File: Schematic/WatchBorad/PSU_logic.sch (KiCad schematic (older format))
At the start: 32 parts, among them J3 TYPE-C-31-M-17, SW1 SW_Push, SW2 SW_Push, U5 BQ21040DBVT, U6 MAX17048G+T10, U7 max16054azt+t, U8 TPS2113APWR

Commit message: Added missed footprints
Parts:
- U6: footprint 21-0168E_T822-3_MXM -> LocalFootprints:MAX17048G
- U8: footprint PowerMuxesFP:TPS2115APWR -> LocalFootprints:TPS2115APWR
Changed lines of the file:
@@
 F 0 "U6" H 4725 6712 60  0000 C CNN
 F 1 "MAX17048G+T10" H 4725 6606 60  0000 C CNN
-F 2 "21-0168E_T822-3_MXM" H 4700 6575 60  0001 C CNN
+F 2 "LocalFootprints:MAX17048G" H 4700 6575 60  0001 C CNN
 F 3 "https://datasheet.lcsc.com/lcsc/2106070437_Maxim-Integrated-MAX17048G-T10_C2682616.pdf" H 4725 6606 60  0001 C CNN
 F 4 "https://lcsc.com/product-detail/PMIC-Battery-Management_Maxim-Integrated-MAX17048G-T10_C2682616.html" H 3925 6325 50  0001 C CNN "lcsc"
@@
 F 0 "U8" H 8375 5062 60  0000 C CNN
 F 1 "TPS2113APWR" H 8375 4956 60  0000 C CNN
-F 2 "PowerMuxesFP:TPS2115APWR" H 8375 4915 60  0001 C CNN
+F 2 "LocalFootprints:TPS2115APWR" H 8375 4915 60  0001 C CNN
 F 3 "https://datasheet.lcsc.com/lcsc/Texas-Instruments-TI-TPS2113APWR_C130052.pdf" H 8375 4175 60  0001 C CNN
 F 4 "https://lcsc.com/product-detail/PMIC-Power-Distribution-Switches_Texas-Instruments_TPS2113APWR_Texas-Instruments-Texas-Instruments-TPS2113APWR_C130052.html" H 8375 4425 50  0001 C CNN "lcsc"

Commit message: Added battery print
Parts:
- BT1: footprint Battery_Holders:Keystone_107_1x23mm-CoinCell -> LocalFootprints:BatteryPads
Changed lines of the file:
@@
 F 0 "BT1" H 1218 6746 50  0000 L CNN
 F 1 "Battery_Cell" H 1218 6655 50  0000 L CNN
-F 2 "Battery_Holders:Keystone_107_1x23mm-CoinCell" V 1100 6710 50  0001 C CNN
+F 2 "LocalFootprints:BatteryPads" V 1100 6710 50  0001 C CNN
 F 3 "https://aliexpress.ru/item/33000396152.html?spm=a2g0o.productlist.0.0.43416af464CXwu&algo_pvid=e6706777-cde6-4668-9867-8799ba4921bb&algo_expid=e6706777-cde6-4668-9867-8799ba4921bb-0&btsid=0b8b037215874644191236041ea897&ws_ab_test=searchweb0_0,searchweb201602_,searchweb201603_" V 1100 6710 50  0001 C CNN
 	1    1100 6650

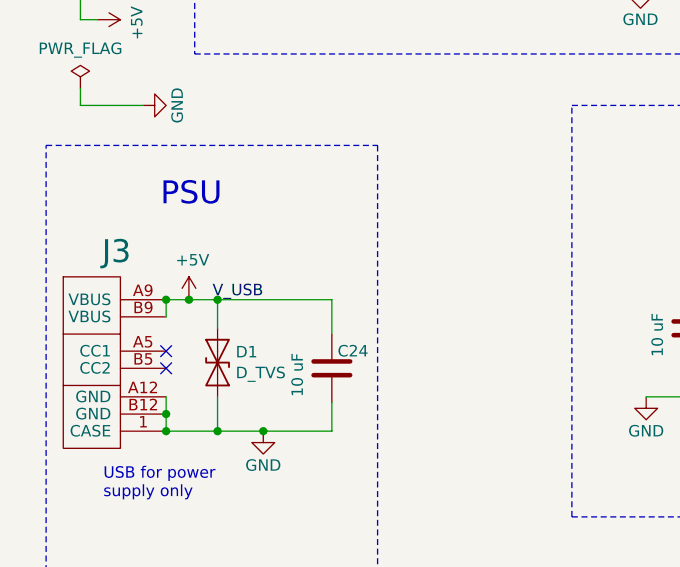
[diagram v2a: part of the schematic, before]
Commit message: Fixed board's proposals. Fixed testpoints' footprint. Fixed DRC violations. Added +5V testpoint
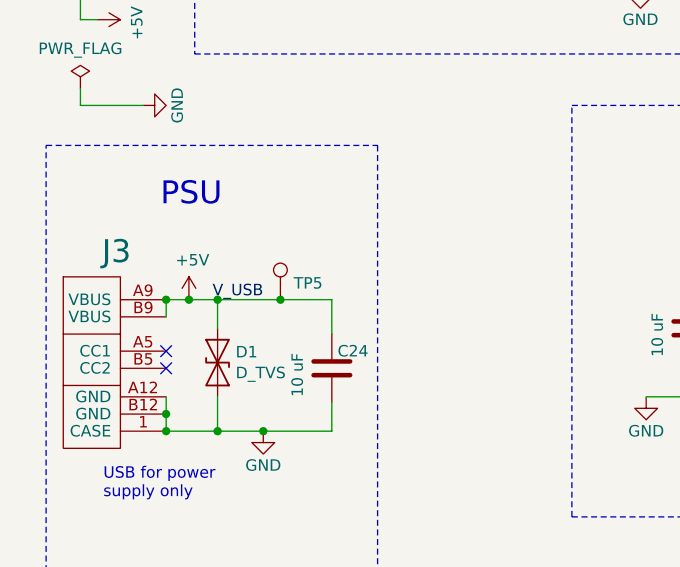
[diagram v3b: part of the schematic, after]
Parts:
- added TP5: TestPoint, TestPoint:TestPoint_Pad_D2.0mm, symbol Connector:TestPoint
- TP11, TP12: footprint Measurement_Points:Measurement_Point_Round-SMD-Pad_Small -> TestPoint:TestPoint_Pad_D2.0mm
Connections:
- wire segments 130 -> 131
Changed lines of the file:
@@
 F 0 "TP11" H 7633 1847 50  0000 L CNN
 F 1 "TestPoint" H 7633 1802 50  0001 L CNN
-F 2 "Measurement_Points:Measurement_Point_Round-SMD-Pad_Small" H 7775 1775 50  0001 C CNN
+F 2 "TestPoint:TestPoint_Pad_D2.0mm" H 7775 1775 50  0001 C CNN
 F 3 "~" H 7775 1775 50  0001 C CNN
 	1    7575 1775
@@
 F 0 "TP12" H 9858 4147 50  0000 L CNN
 F 1 "TestPoint" H 9858 4102 50  0001 L CNN
-F 2 "Measurement_Points:Measurement_Point_Round-SMD-Pad_Small" H 10000 4075 50  0001 C CNN
+F 2 "TestPoint:TestPoint_Pad_D2.0mm" H 10000 4075 50  0001 C CNN
 F 3 "~" H 10000 4075 50  0001 C CNN
 	1    9800 4075
@@
 	1775 4250 1775 4400
 Wire Wire Line
-	1275 4250 1775 4250
+	1275 4250 1550 4250
 $Comp
 L Device:C C?
@@
 	9200 4575 9200 4675
 Connection ~ 9200 4675
+$Comp
+L Connector:TestPoint TP?
+U 1 1 60EA81F2
+P 1550 4250
+AR Path="/5E9C1C3A/60EA81F2" Ref="TP?"  Part="1"
+AR Path="/5ED3F98E/60EA81F2" Ref="TP?"  Part="1"
+AR Path="/5F913559/60EA81F2" Ref="TP5"  Part="1"
+F 0 "TP5" H 1608 4322 50  0000 L CNN
+F 1 "TestPoint" H 1608 4277 50  0001 L CNN
+F 2 "TestPoint:TestPoint_Pad_D2.0mm" H 1750 4250 50  0001 C CNN
+F 3 "~" H 1750 4250 50  0001 C CNN
+	1    1550 4250
+	1    0    0    -1
+$EndComp
+Connection ~ 1550 4250
+Wire Wire Line
+	1550 4250 1775 4250
 $EndSCHEMATC

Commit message: Added new DCDC and radio antenna from Rulepas [SCHECMATIC]
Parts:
- removed R25: 10k, Resistor_SMD:R_0603_1608Metric, symbol Device:R
- removed VT3: HX2301A, TO_SOT_Packages_SMD:SOT-23, symbol MosfetLocal:HX2301A
- added C?: 100 nF, Capacitor_SMD:C_0603_1608Metric, symbol Device:C
- added R? (x2): 10k, Resistor_SMD:R_0603_1608Metric, symbol Device:R
- added U?: M41T62Q6F, QFN50P300X300X100-17N, symbol M41T62Q6F:M41T62Q6F
- added Y?: Crystal_Small, Crystal:Crystal_SMD_3215-2Pin_3.2x1.5mm, symbol Device:Crystal_Small
- U6: symbol WatchBorad-rescue:MAX17048G+T10-BatteryManagmentLocal-WatchBorad-rescue -> WatchBorad-rescue:MAX17048G+T10-BatteryManagmentLocal-WatchBorad-rescue-WatchBorad-rescue
- U8: symbol WatchBorad-rescue:TPS2113APWR-PowerMuxes-WatchBorad-rescue -> WatchBorad-rescue:TPS2113APWR-PowerMuxes-WatchBorad-rescue-WatchBorad-rescue
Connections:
- net labels added: I2C_SCL_STBY, I2C_SDA_STBY, PWR_SW_EN_N, XI_RTC, XO_RTC
- net labels removed: V_Battery_P_SW
- wire segments 131 -> 145
- no-connect marks 5 -> 7
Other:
- note added: "32.768 KHz\n"
- note added: "RTC_I2C"
- note added: "default level is "0""
- note added: "internal PU\n"
- note removed: "PUs next to MCU\n"
- moved on the sheet: C25, C26, C28, C29, C30, C31, R15, R16, R17, R18, R20, R21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

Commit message: Added schematic files annotations [SCHEMATIC]
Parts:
- gave numbers to parts that had none: 5
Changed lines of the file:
@@
 P 8225 4200
 AR Path="/5E9B1DCE/61A98A66" Ref="#PWR?"  Part="1"
-AR Path="/5F913559/61A98A66" Ref="#PWR?"  Part="1"
-F 0 "#PWR?" H 8225 3950 50  0001 C CNN
+AR Path="/5F913559/61A98A66" Ref="#PWR07"  Part="1"
+F 0 "#PWR07" H 8225 3950 50  0001 C CNN
 F 1 "GND" H 8230 4027 50  0000 C CNN
 F 2 "" H 8225 4200 50  0001 C CNN
@@
 P 9475 3050
 AR Path="/5E9B1DCE/61A98A80" Ref="U?"  Part="1"
-AR Path="/5F913559/61A98A80" Ref="U?"  Part="1"
-F 0 "U?" H 9475 4220 50  0000 C CNN
+AR Path="/5F913559/61A98A80" Ref="U10"  Part="1"
+F 0 "U10" H 9475 4220 50  0000 C CNN
 F 1 "M41T62Q6F" H 9475 4129 50  0000 C CNN
 F 2 "QFN50P300X300X100-17N" H 9475 3050 50  0001 L BNN
@@
 P 10325 3600
 AR Path="/5E9B1DCE/61A98A89" Ref="#PWR?"  Part="1"
-AR Path="/5F913559/61A98A89" Ref="#PWR?"  Part="1"
-F 0 "#PWR?" H 10325 3350 50  0001 C CNN
+AR Path="/5F913559/61A98A89" Ref="#PWR051"  Part="1"
+F 0 "#PWR051" H 10325 3350 50  0001 C CNN
 F 1 "GND" H 10330 3427 50  0000 C CNN
 F 2 "" H 10325 3600 50  0001 C CNN
@@
 AR Path="/5E9B1DCE/61A98A8F" Ref="C?"  Part="1"
 AR Path="/61A98A8F" Ref="C?"  Part="1"
-AR Path="/5F913559/61A98A8F" Ref="C?"  Part="1"
-F 0 "C?" H 10500 3400 50  0000 L CNN
+AR Path="/5F913559/61A98A8F" Ref="C6"  Part="1"
+F 0 "C6" H 10500 3400 50  0000 L CNN
 F 1 "100 nF" H 10450 3300 50  0000 L CNN
 F 2 "Capacitor_SMD:C_0603_1608Metric" H 10363 3225 50  0001 C CNN
@@
 P 10375 2400
 AR Path="/5E9B1DCE/61A98AAA" Ref="R?"  Part="1"
-AR Path="/5F913559/61A98AAA" Ref="R?"  Part="1"
-F 0 "R?" H 10445 2446 50  0000 L CNN
+AR Path="/5F913559/61A98AAA" Ref="R2"  Part="1"
+F 0 "R2" H 10445 2446 50  0000 L CNN
 F 1 "10k" H 10445 2355 50  0000 L CNN
 F 2 "Resistor_SMD:R_0603_1608Metric" V 10305 2400 50  0001 C CNN
@@
 P 8325 2300
 AR Path="/5E9B1DCE/61A98AB0" Ref="R?"  Part="1"
-AR Path="/5F913559/61A98AB0" Ref="R?"  Part="1"
-F 0 "R?" H 8395 2346 50  0000 L CNN
+AR Path="/5F913559/61A98AB0" Ref="R1"  Part="1"
+F 0 "R1" H 8395 2346 50  0000 L CNN
 F 1 "10k" H 8395 2255 50  0000 L CNN
 F 2 "Resistor_SMD:R_0603_1608Metric" V 8255 2300 50  0001 C CNN
@@
 AR Path="/5F7F86D0/61AF93FF" Ref="#PWR?"  Part="1"
 AR Path="/5ED3F98E/61AF93FF" Ref="#PWR?"  Part="1"
-AR Path="/5F913559/61AF93FF" Ref="#PWR?"  Part="1"
-F 0 "#PWR?" H 8625 1950 50  0001 C CNN
+AR Path="/5F913559/61AF93FF" Ref="#PWR012"  Part="1"
+F 0 "#PWR012" H 8625 1950 50  0001 C CNN
 F 1 "+BATT" H 8640 2273 50  0000 C CNN
 F 2 "" H 8625 2100 50  0001 C CNN
@@
 AR Path="/5F7F86D0/61AFA253" Ref="#PWR?"  Part="1"
 AR Path="/5ED3F98E/61AFA253" Ref="#PWR?"  Part="1"
-AR Path="/5F913559/61AFA253" Ref="#PWR?"  Part="1"
-F 0 "#PWR?" H 10575 1950 50  0001 C CNN
+AR Path="/5F913559/61AFA253" Ref="#PWR056"  Part="1"
+F 0 "#PWR056" H 10575 1950 50  0001 C CNN
 F 1 "+BATT" H 10590 2273 50  0000 C CNN
 F 2 "" H 10575 2100 50  0001 C CNN
@@
 AR Path="/5F7F86D0/61AFA5F0" Ref="#PWR?"  Part="1"
 AR Path="/5ED3F98E/61AFA5F0" Ref="#PWR?"  Part="1"
-AR Path="/5F913559/61AFA5F0" Ref="#PWR?"  Part="1"
-F 0 "#PWR?" H 10325 2950 50  0001 C CNN
+AR Path="/5F913559/61AFA5F0" Ref="#PWR044"  Part="1"
+F 0 "#PWR044" H 10325 2950 50  0001 C CNN
 F 1 "+BATT" H 10340 3273 50  0000 C CNN
 F 2 "" H 10325 3100 50  0001 C CNN
@@
 $EndComp
 $Comp
-L Device:Crystal_Small Y?
+L Device:Crystal_Small Y1
 U 1 1 61B0CA61
 P 8200 3300
-F 0 "Y?" V 8250 3500 50  0000 R CNN
+F 0 "Y1" V 8250 3500 50  0000 R CNN
 F 1 "Crystal_Small" V 8150 3900 50  0000 R CNN
 F 2 "Crystal:Crystal_SMD_3215-2Pin_3.2x1.5mm" H 8200 3300 50  0001 C CNN

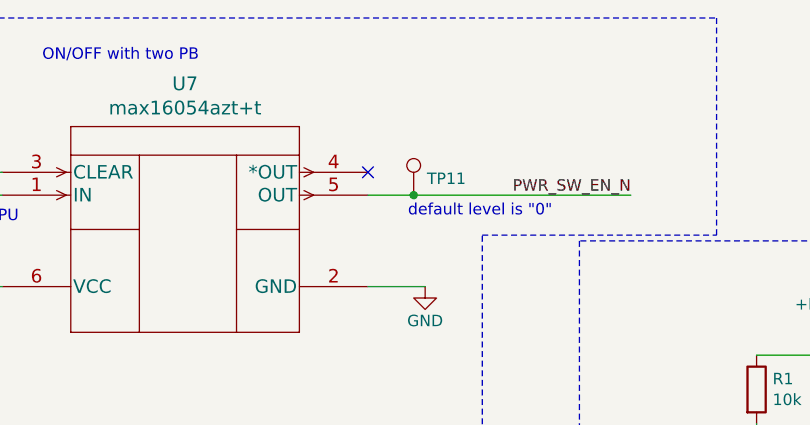
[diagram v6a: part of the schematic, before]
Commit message: Added testpoint to the on/off circuit [PCB][SCHEMATIC]
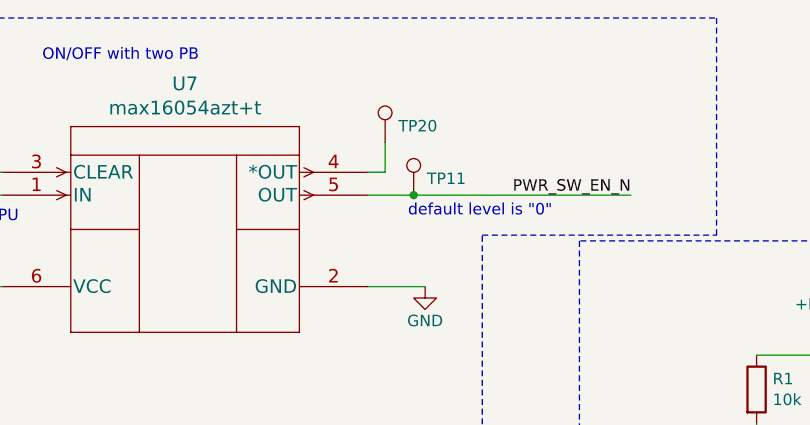
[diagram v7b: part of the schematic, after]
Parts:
- added TP20: TestPoint, TestPoint:TestPoint_Pad_D2.0mm, symbol Connector:TestPoint
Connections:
- wire segments 145 -> 147
- no-connect marks 7 -> 6
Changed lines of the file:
@@
 	1    0    0    -1
 $EndComp
-NoConn ~ 6625 1350
 Text Notes 6800 1550 0    50   ~ 0
 default level is "0"
@@
 NoConn ~ 10175 2350
 NoConn ~ 8775 2450
+$Comp
+L Connector:TestPoint TP20
+U 1 1 6186C8E6
+P 6700 1220
+F 0 "TP20" H 6758 1292 50  0000 L CNN
+F 1 "TestPoint" H 6758 1247 50  0001 L CNN
+F 2 "TestPoint:TestPoint_Pad_D2.0mm" H 6900 1220 50  0001 C CNN
+F 3 "~" H 6900 1220 50  0001 C CNN
+	1    6700 1220
+	1    0    0    -1
+$EndComp
+Wire Wire Line
+	6625 1350 6700 1350
+Wire Wire Line
+	6700 1220 6700 1350
 $EndSCHEMATC

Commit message: Added missed components to the symbol lists [SCHEMATIC]
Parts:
- C25, C26, C27, C29, C30, C31, C6: lcsc (none) -> https://lcsc.com/product-detail/Multilayer-Ceramic-Capacito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
- Y1: LCSC https://lcsc.com/product-detail/Crystals_TKD-SF32WK32768D31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 -> (none); lcsc (none) -> https://lcsc.com/product-detail/Crystals_TKD-SF32WK32768D31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
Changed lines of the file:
@@
 F 2 "Capacitor_SMD:C_0603_1608Metric" H 4888 2025 50  0001 C CNN
 F 3 "~" H 4850 2175 50  0001 C CNN
+F 4 "https://lcsc.com/product-detail/Multilayer-Ceramic-Capacitors-MLCC-SMD-SMT_YAGEO-CC0603KRX7R9BB104_C14663.html" H 4850 2175 50  0001 C CNN "lcsc"
 	1    4850 2175
 	1    0    0    -1
@@
 F 2 "Capacitor_SMD:C_0603_1608Metric" H 7288 5625 50  0001 C CNN
 F 3 "~" H 7250 5775 50  0001 C CNN
+F 4 "https://lcsc.com/product-detail/Multilayer-Ceramic-Capacitors-MLCC-SMD-SMT_YAGEO-CC0603KRX7R9BB104_C14663.html" H 7250 5775 50  0001 C CNN "lcsc"
 	1    7250 5775
 	1    0    0    -1
@@
 F 2 "Capacitor_SMD:C_0603_1608Metric" H 7888 5625 50  0001 C CNN
 F 3 "~" H 7850 5775 50  0001 C CNN
+F 4 "https://lcsc.com/product-detail/Multilayer-Ceramic-Capacitors-MLCC-SMD-SMT_YAGEO-CC0603KRX7R9BB104_C14663.html" H 7850 5775 50  0001 C CNN "lcsc"
 	1    7850 5775
 	1    0    0    -1
@@
 F 2 "Capacitor_SMD:C_0603_1608Metric" H 1763 2450 50  0001 C CNN
 F 3 "~" H 1725 2600 50  0001 C CNN
+F 4 "https://lcsc.com/product-detail/Multilayer-Ceramic-Capacitors-MLCC-SMD-SMT_YAGEO-CC0603KRX7R9BB104_C14663.html" H 1725 2600 50  0001 C CNN "lcsc"
 	1    1725 2600
 	1    0    0    -1
@@
 F 2 "Capacitor_SMD:C_0603_1608Metric" H 2063 2450 50  0001 C CNN
 F 3 "~" H 2025 2600 50  0001 C CNN
+F 4 "https://lcsc.com/product-detail/Multilayer-Ceramic-Capacitors-MLCC-SMD-SMT_YAGEO-CC0603KRX7R9BB104_C14663.html" H 2025 2600 50  0001 C CNN "lcsc"
 	1    2025 2600
 	1    0    0    -1
@@
 F 2 "Capacitor_SMD:C_0603_1608Metric" H 3013 6725 50  0001 C CNN
 F 3 "~" H 2975 6875 50  0001 C CNN
+F 4 "https://lcsc.com/product-detail/Multilayer-Ceramic-Capacitors-MLCC-SMD-SMT_YAGEO-CC0603KRX7R9BB104_C14663.html" H 2975 6875 50  0001 C CNN "lcsc"
 	1    2975 6875
 	1    0    0    -1
@@
 F 2 "Capacitor_SMD:C_0603_1608Metric" H 10363 3225 50  0001 C CNN
 F 3 "~" H 10325 3375 50  0001 C CNN
+F 4 "https://lcsc.com/product-detail/Multilayer-Ceramic-Capacitors-MLCC-SMD-SMT_YAGEO-CC0603KRX7R9BB104_C14663.html" H 10325 3375 50  0001 C CNN "lcsc"
 	1    10325 3375
 	1    0    0    -1
@@
 F 2 "Crystal:Crystal_SMD_3215-2Pin_3.2x1.5mm" H 8200 3300 50  0001 C CNN
 F 3 "https://datasheet.lcsc.com/lcsc/2104141604_TKD-SF32WK32768D31T002_C271654.pdf" H 8200 3300 50  0001 C CNN
-F 4 "https://lcsc.com/product-detail/Crystals_TKD-SF32WK32768D31T002_C271654.html" V 8200 3300 50  0001 C CNN "LCSC"
+F 4 "" V 8200 3300 50  0001 C CNN "LCSC"
+F 5 "https://lcsc.com/product-detail/Crystals_TKD-SF32WK32768D31T002_C271654.html" H 8200 3300 50  0001 C CNN "lcsc"
 	1    8200 3300
 	0    -1   -1   0
